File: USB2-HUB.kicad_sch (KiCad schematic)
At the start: 42 parts, among them J11 USB_OTG, J13 BM04B-GHS-TBT(LF)(SN)(N), J14 BM04B-GHS-TBT(LF)(SN)(N), J18 BM04B-GHS-TBT(LF)(SN)(N), J21 BM04B-GHS-TBT(LF)(SN)(N), U10 AP22653W6, U13 FSUSB42MUX, U4 TPD4EUSB30, U6 USB2514B-I/M2, U7 AP22653W6, Y1 24MHz

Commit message: library management
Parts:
- R31: footprint (none) -> Resistor_SMD:R_0402_1005Metric
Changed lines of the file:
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@@
       (effects (font (size 1.143 1.143)))
     )
-    (property "Footprint" "" (id 2) (at 217.17 57.15 0)
+    (property "Footprint" "Resistor_SMD:R_0402_1005Metric" (id 2) (at 217.17 57.15 0)
       (effects (font (size 1.016 1.016)) hide)
     )

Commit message: updating readme and some layout
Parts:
- removed C16, C50: 100uF, Capacitor_Tantalum_SMD:CP_EIA-7343-31_Kemet-D, symbol Device:CP
- removed J11: USB_OTG, CM4IO:USB_Micro-B_EDAC_UCON00686, symbol Connector:USB_OTG
- added J3: USB4085-GF-A_REVA, Open-HD:GCT_USB4085-GF-A_REVA, symbol USB4085-GF-A_REVA:USB4085-GF-A_REVA
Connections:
- net at R8.1: now also J3.A4 (VBUS), J3.A9 (VBUS), J3.B4 (VBUS), J3.B9 (VBUS)
- new net: J3.A1 (GND), J3.A12 (GND), J3.B1 (GND), J3.B12 (GND)
- new net: J3.P1 (SHELL), J3.P2 (SHELL), J3.P3 (SHELL), J3.P4 (SHELL)
- no-connect marks 4 -> 3

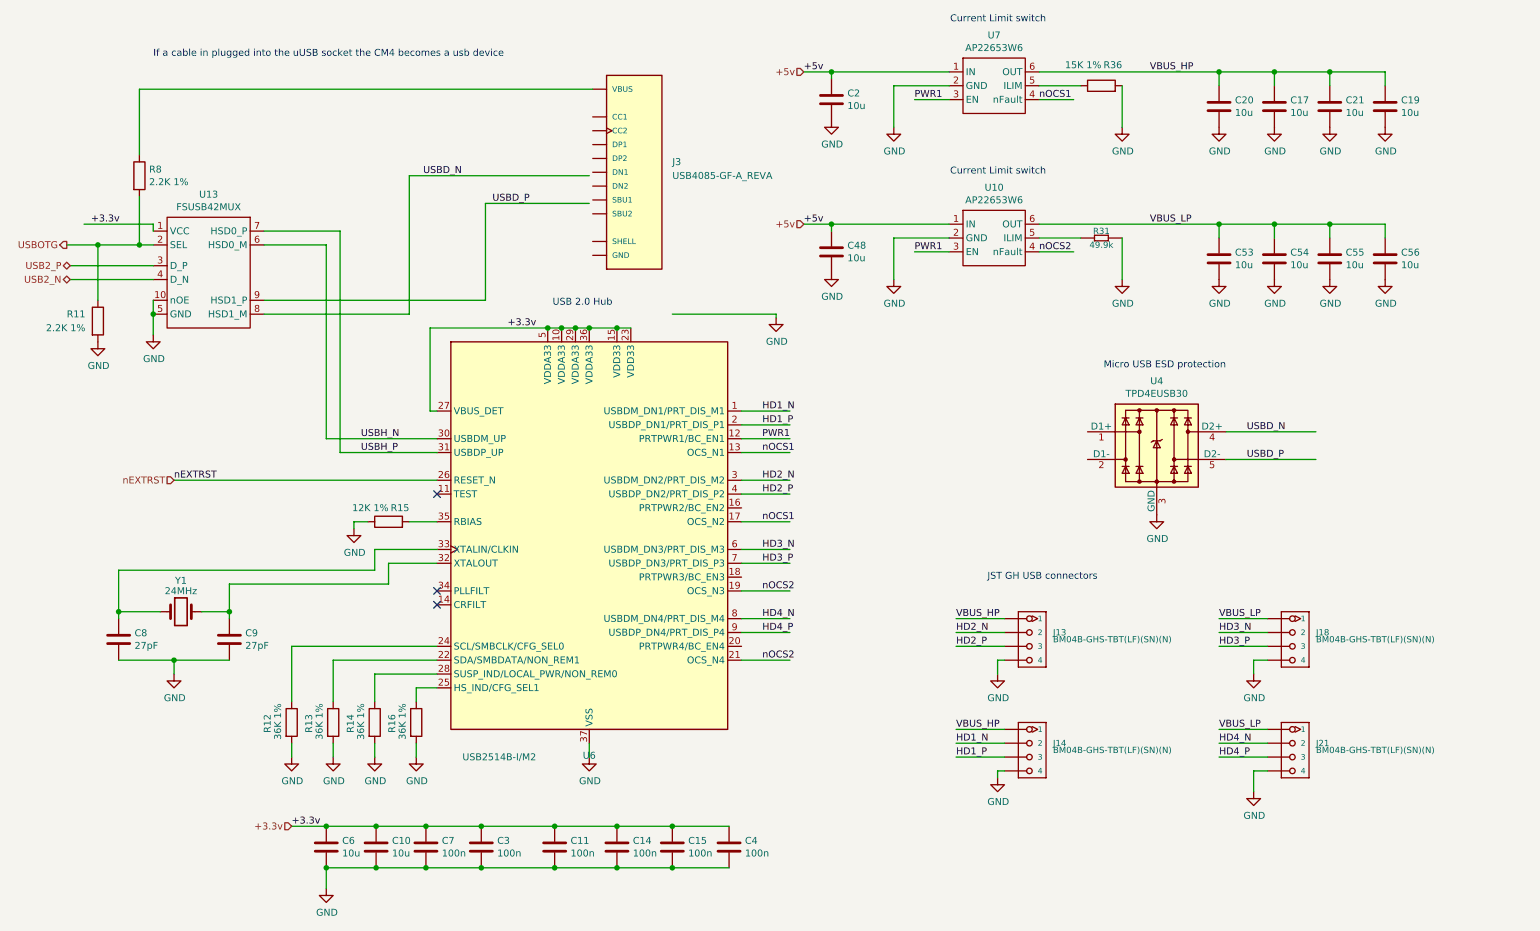
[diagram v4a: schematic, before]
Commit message: started routing USB, added usb power switches, routing some USB-C
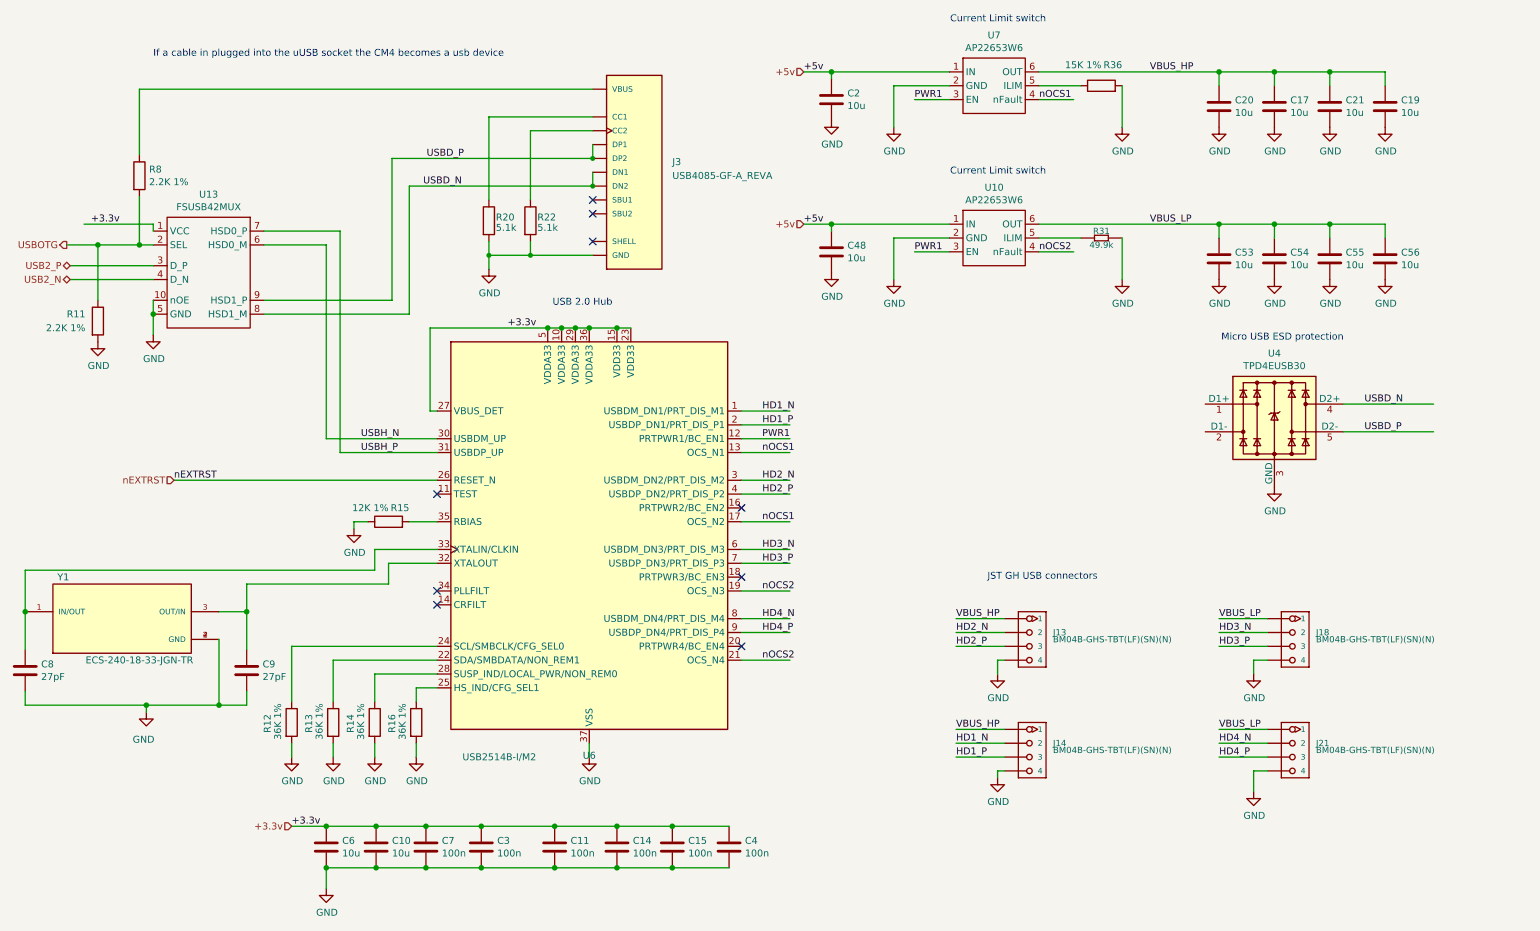
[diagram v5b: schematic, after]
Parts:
- removed Y1: 24MHz, Crystal:Crystal_SMD_HC49-SD, symbol Device:Crystal
- added R20, R22: 5.1k, Resistor_SMD:R_0402_1005Metric, symbol Device:R
- added Y1: ECS-240-18-33-JGN-TR, XTAL_ECS-240-18-33-JGN-TR, symbol ECS-240-18-33-JGN-TR:ECS-240-18-33-JGN-TR
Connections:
- net GND: now also J3.A1 (GND), J3.A12 (GND), J3.B1 (GND), J3.B12 (GND), R20.2, R22.2, Y1.2 (GND), Y1.4 (GND)
- net USBD_N: now also J3.A7 (DN1), J3.B7 (DN2)
- net USBD_P: now also J3.A6 (DP1), J3.B6 (DP2)
- net at C9.1, U6.32 (XTALOUT): now also Y1.3 (OUT/IN)
- net at C8.1, U6.33 (XTALIN/CLKIN): now also Y1.1 (IN/OUT)
- net at J3.A5 (CC1): now also R20.1
- net at J3.B5 (CC2): now also R22.1
- no-connect marks 3 -> 9
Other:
- moved on the sheet: C8, C9, U4

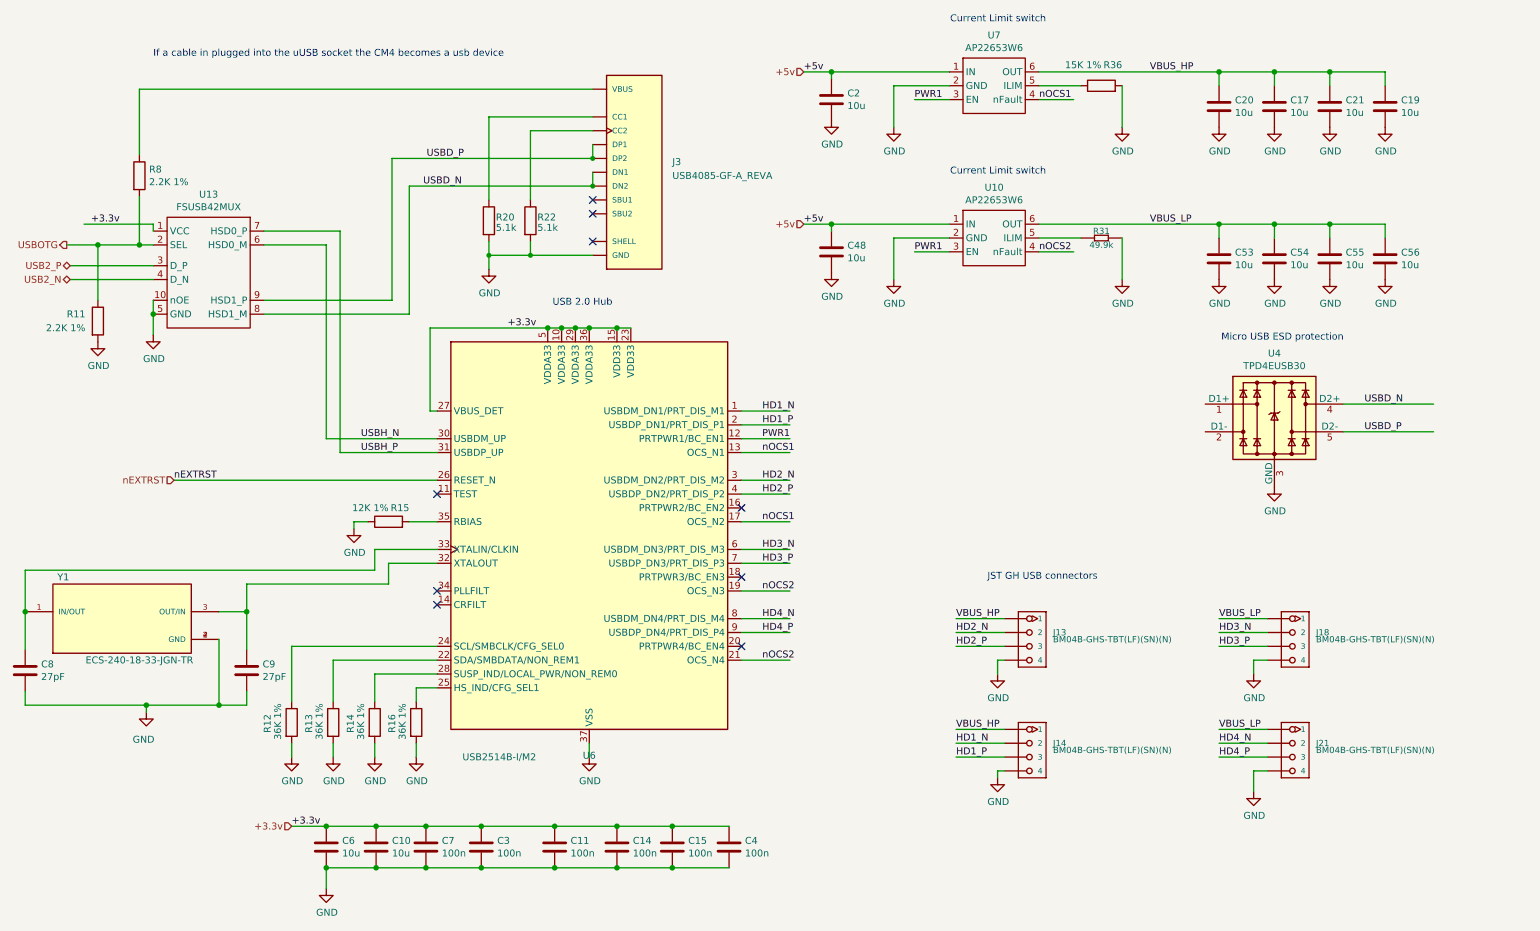
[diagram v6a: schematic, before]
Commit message: Changed footprint to match CM4, removed Ethernet and HDMI
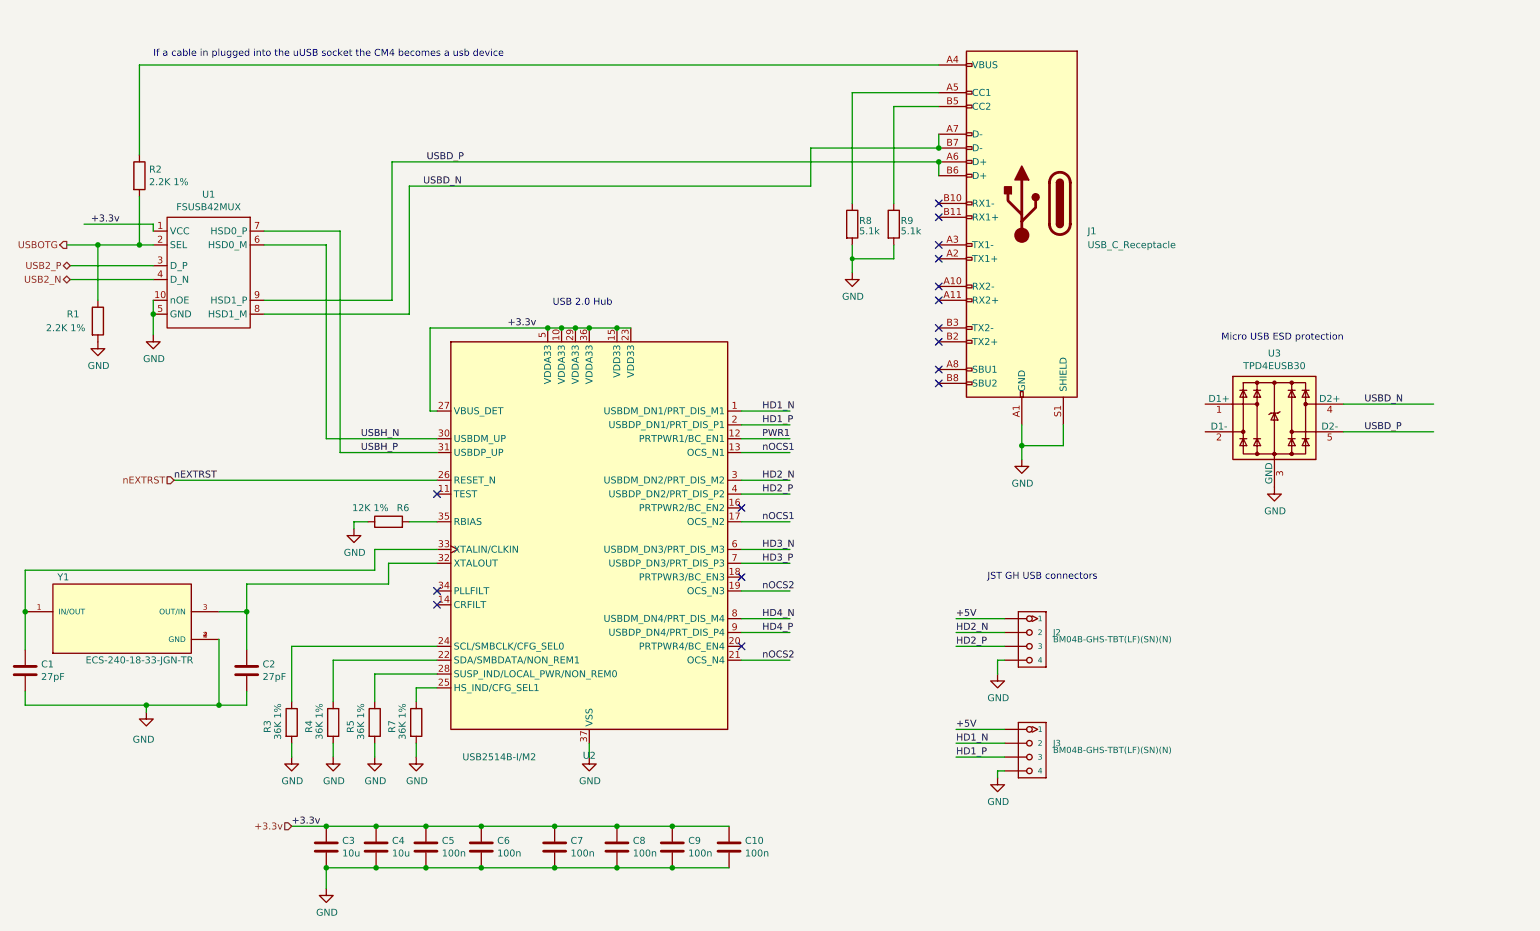
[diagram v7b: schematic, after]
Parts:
- removed C17, C19, C2, C20, C21, C48, C53, C54, C55, C56: 10u, Capacitor_SMD:C_0805_2012Metric, symbol Device:C
- removed J18, J21: BM04B-GHS-TBT(LF)(SN)(N), Connectors_JST:JST_GH_SM04B-GHS-TB_04x1.25mm_Angled, symbol OPL_Connector:GROVE-CONNECTOR-SMD-90D_4+2P-2.0_
- removed J3: USB4085-GF-A_REVA, Open-HD:GCT_USB4085-GF-A_REVA, symbol USB4085-GF-A_REVA:USB4085-GF-A_REVA
- removed R31: 49.9k, Resistor_SMD:R_0402_1005Metric, symbol OPL_Resistor:SMD-RES-49.9R-1%-1_16W_0402_
- removed R36: 15K 1%, Resistor_SMD:R_0402_1005Metric, symbol Device:R
- removed U10, U7: AP22653W6, Package_TO_SOT_SMD:SOT-23-6, symbol CM4IO:AP2553W6
- added J1: USB_C_Receptacle, CM4IO:USB-C-SMD_TYPE-C-USB-17, symbol Connector:USB_C_Receptacle
- renumbered C8 to C1, C4 to C10, C9 to C2, C6 to C3, C10 to C4, C7 to C5, C3 to C6, C11 to C7, C14 to C8, C15 to C9, J13 to J2, J14 to J3, R11 to R1, R8 to R2, R12 to R3, R13 to R4, R14 to R5, R15 to R6, R16 to R7, R20 to R8, R22 to R9, U13 to U1, U6 to U2, U4 to U3
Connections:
- net GND: now also J1.A1 (GND), J1.A12 (GND), J1.B1 (GND), J1.B12 (GND), J1.S1 (SHIELD)
- net USBD_N: now also J1.A7 (D-), J1.B7 (D-)
- net USBD_P: now also J1.A6 (D+), J1.B6 (D+)
- net at R2.1: now also J1.A4 (VBUS), J1.A9 (VBUS), J1.B4 (VBUS), J1.B9 (VBUS)
- net at R8.1: now also J1.A5 (CC1)
- net at R9.1: now also J1.B5 (CC2)
- net VBUS_HP renamed +5V
- no-connect marks 9 -> 16
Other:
- note removed: "Current Limit switch"
- moved on the sheet: R8, R9

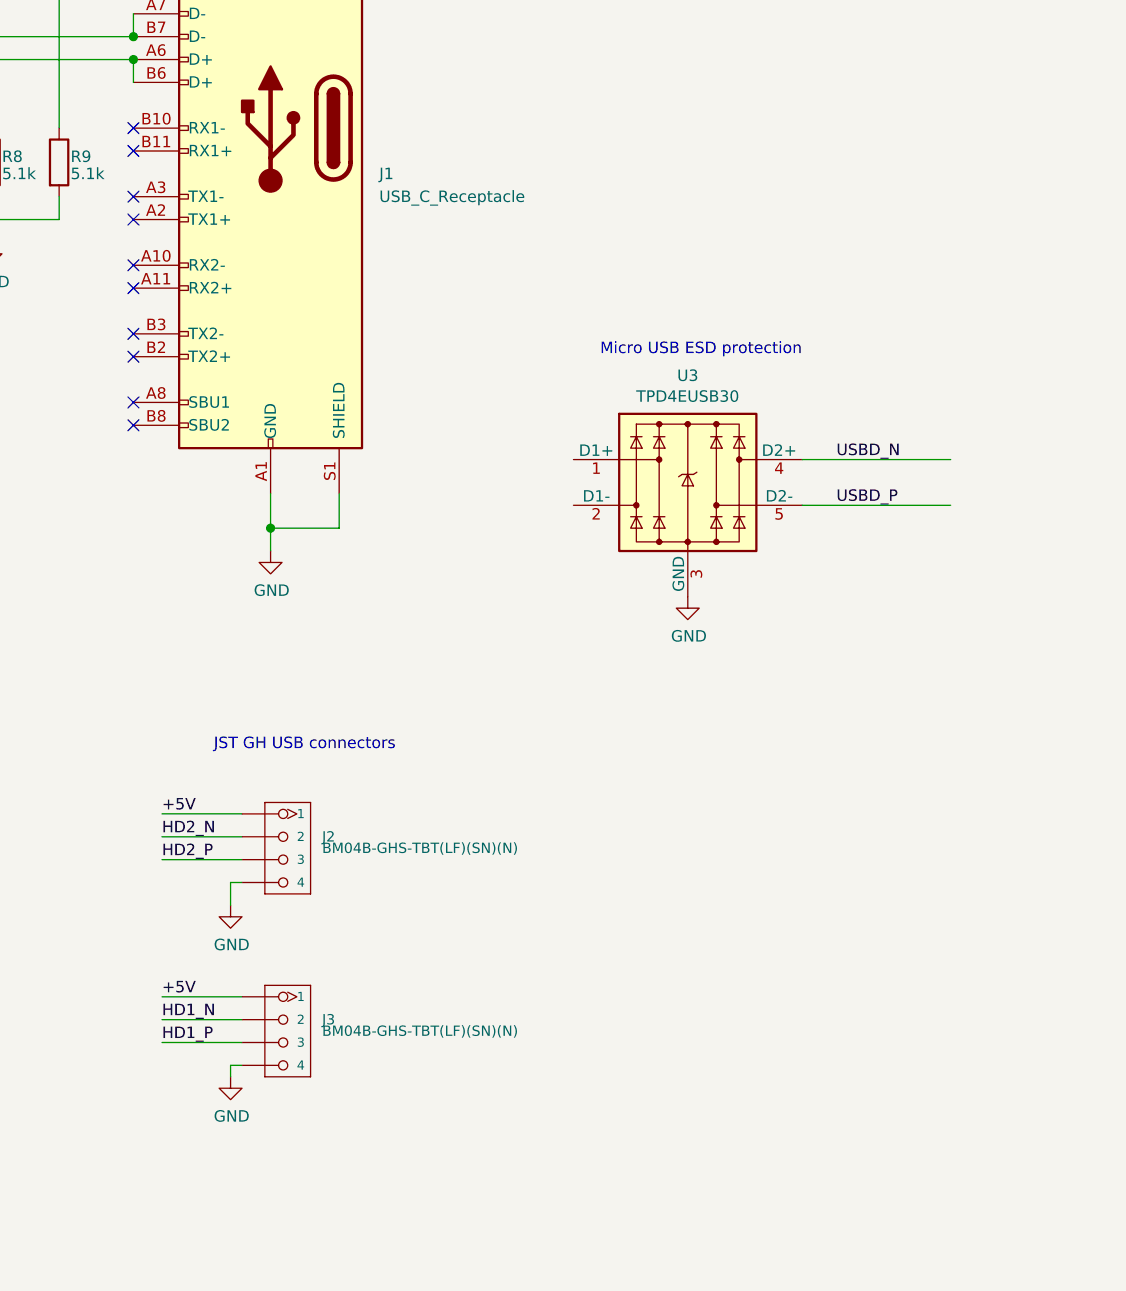
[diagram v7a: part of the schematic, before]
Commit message: additional layout, power circuitry
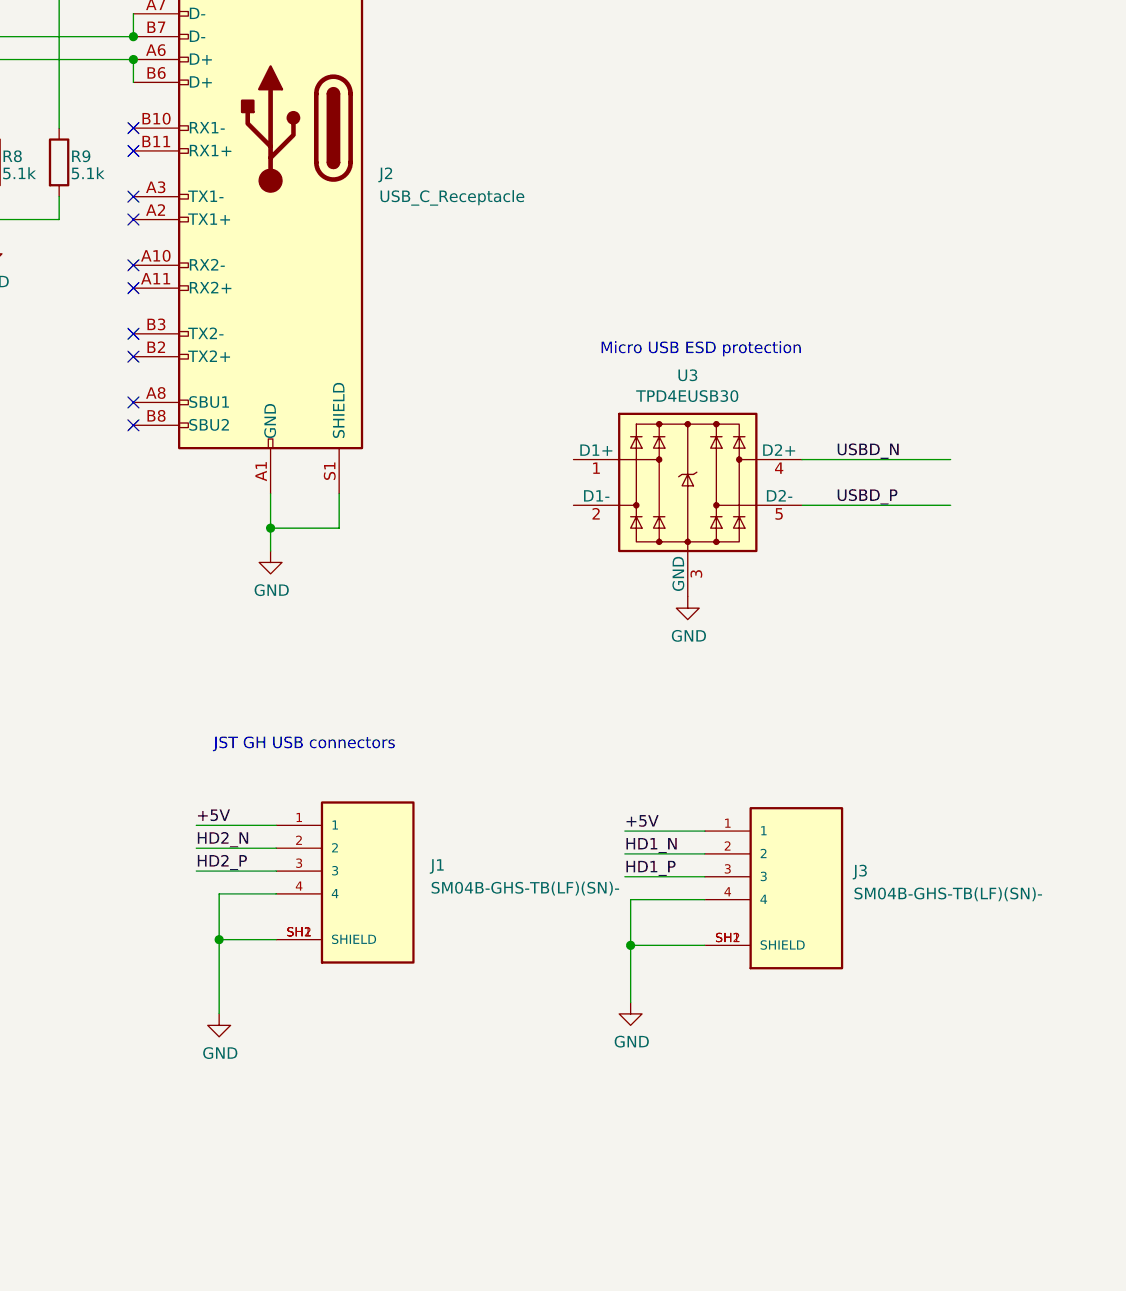
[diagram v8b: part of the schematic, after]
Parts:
- removed J2, J3: BM04B-GHS-TBT(LF)(SN)(N), Connectors_JST:JST_GH_SM04B-GHS-TB_04x1.25mm_Angled, symbol OPL_Connector:GROVE-CONNECTOR-SMD-90D_4+2P-2.0_
- added J1, J3: SM04B-GHS-TB(LF)(SN)-, JST_SM04B-GHS-TB(LF)(SN)-, symbol SM04B-GHS-TB_LF__SN_-:SM04B-GHS-TB(LF)(SN)-
- renumbered J1 to J2
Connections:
- net +5V: now also J1.1, J3.1
- net GND: now also J1.4, J1.SH1 (SHIELD), J1.SH2 (SHIELD), J3.4, J3.SH1 (SHIELD), J3.SH2 (SHIELD)
- net HD1_N: now also J3.2
- net HD1_P: now also J3.3
- net HD2_N: now also J1.2
- net HD2_P: now also J1.3
